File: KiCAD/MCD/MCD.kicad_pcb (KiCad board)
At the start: 2 copper layers, 197 x 101.5 mm, 76 parts, among them J1 DBUS_LOW, J2 DBUS_HIGH, J3 ABUS, J4 POWER, J5 JTAG, J6 Conn_01x02_Male, J7 DUART A, J8 DUART B, SW1 SW_Push, U1 XC9572XL-10VQG44C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

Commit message: control bus almost done
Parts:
- C1, C10, C11, C13, C2, C3, C4, C8, R10, R11, R14, R3, R4, R5, R6, R7: moved to B.Cu
- moved D2 55.6 mm to (106.5, 115.0), turned to 0 degrees
- moved D3 53.6 mm to (106.5, 118.0), turned to 0 degrees
- moved D4 51.9 mm to (106.5, 121.0), turned to 0 degrees
- moved D5 50.5 mm to (106.5, 124.0), turned to 0 degrees
- moved R17 50.2 mm to (110.9, 115.0), turned to 180 degrees
- moved D6 49.5 mm to (106.5, 127.0), turned to 0 degrees
- moved D7 48.8 mm to (106.5, 130.0), turned to 0 degrees
- moved R18 48.0 mm to (111.0, 118.0), turned to 180 degrees
- moved R19 46.1 mm to (111.0, 121.0), turned to 180 degrees
- moved R20 44.5 mm to (111.0, 124.0), turned to 180 degrees
- moved R21 43.3 mm to (111.0, 127.0), turned to 180 degrees
- moved R22 42.5 mm to (111.0, 130.0), turned to 180 degrees
- moved C8 10.7 mm to (253.0, 146.0)
- moved C2 10.7 mm to (280.0, 145.8)
- moved C10 10.5 mm to (198.5, 146.3)
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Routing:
- net RAMHCE: track 0.00 -> 190.1 mm, vias 0 -> 1
- net RAMHOE: track 0.00 -> 186.5 mm, vias 0 -> 1
- net ROMHCE: track 0.00 -> 160.5 mm, vias 0 -> 1
- net ROMHOE: track 0.00 -> 158.1 mm, vias 0 -> 1
- net RAMLCE: track 0.00 -> 134.4 mm, vias 0 -> 1
- net RAMLOE: track 0.00 -> 132.4 mm, vias 0 -> 1
- net RAMLCE2: track 162.4 -> 118.6 mm
- net R/W: track 248.4 -> 291.9 mm
- net RAMHCE2: track 208.0 -> 171.2 mm
- net ROMLOE: track 84.7 -> 110.6 mm, vias 3 -> 1
- net ROMLCE: track 87.9 -> 112.4 mm
- net +5V: track 86.1 -> 85.3 mm
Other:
- board size 197 x 101.5 mm -> 196.5 x 109.5 mm
- board text added: "GEORGE YACOUBIAN LETU SP 2024 GeorgeOS Single Board Computer - ADD FEET - ADD VETRIUM MARKERS - ADD ROUNDED CORNERS"
- board text removed: "GEORGE YACOUBIAN LETU SP 2024 GeorgeOS Single Board Computer - ADD FEET - ADD VETRIUM MARKERS - 4 LAYER?"

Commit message: update
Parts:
- moved J5 35.5 mm to (107.0, 136.5), turned to 90 degrees
- moved C20 27.0 mm to (118.0, 174.5), turned to 0 degrees
- moved U10 22.0 mm to (119.0, 171.0), turned to -90 degrees
- moved D3 15.1 mm to (117.8, 108.0)
- moved D4 15.1 mm to (117.8, 111.0)
- moved D5 15.1 mm to (117.8, 114.0)
- moved D6 15.1 mm to (117.8, 117.0)
- moved D7 15.1 mm to (117.8, 120.0)
- moved R17 15.1 mm to (122.2, 105.0)
- moved D2 15.1 mm to (117.7, 105.0)
- moved R18 15.1 mm to (122.2, 108.0)
- moved R19 15.1 mm to (122.2, 111.0)
- moved R20 15.1 mm to (122.2, 114.0)
- moved R21 15.1 mm to (122.2, 117.0)
- moved R22 15.1 mm to (122.2, 120.0)
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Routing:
- net RAMHCE2: track 171.2 -> 226.2 mm, vias 1 -> 2
- net RAMHCE: track 190.1 -> 237.1 mm
- net TDO: track 0.00 -> 46.9 mm, vias 0 -> 2
- net RAMHOE: track 186.5 -> 232.9 mm
- net SRESET: track 0.00 -> 31.3 mm, vias 0 -> 2
- net ROMHOE: track 158.1 -> 187.7 mm
- net BRESET: track 0.00 -> 24.2 mm, vias 0 -> 1
- net ROMHCE: track 160.5 -> 183.8 mm
- net TMS: track 0.00 -> 22.7 mm
- net TDI: track 0.00 -> 19.2 mm
- net RAMLOE: track 132.4 -> 150.8 mm
- net TCK: track 0.00 -> 18.0 mm
- net +5V: track 85.3 -> 102.9 mm, vias 6 -> 8
- net RAMLCE: track 134.4 -> 151.1 mm
- net RAMLCE2: track 118.6 -> 134.4 mm
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
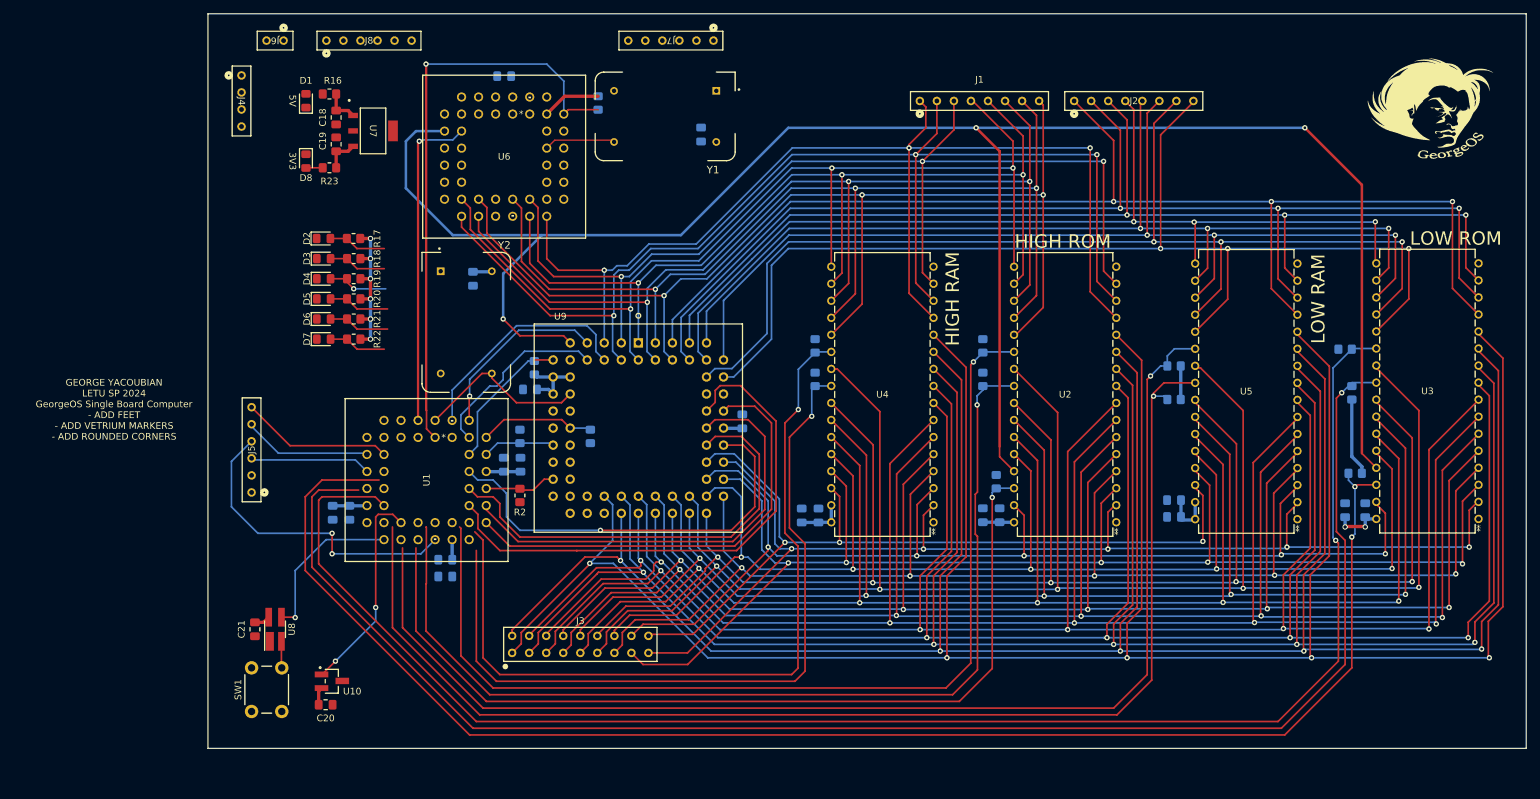
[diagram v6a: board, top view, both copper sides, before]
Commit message: everything but power connected
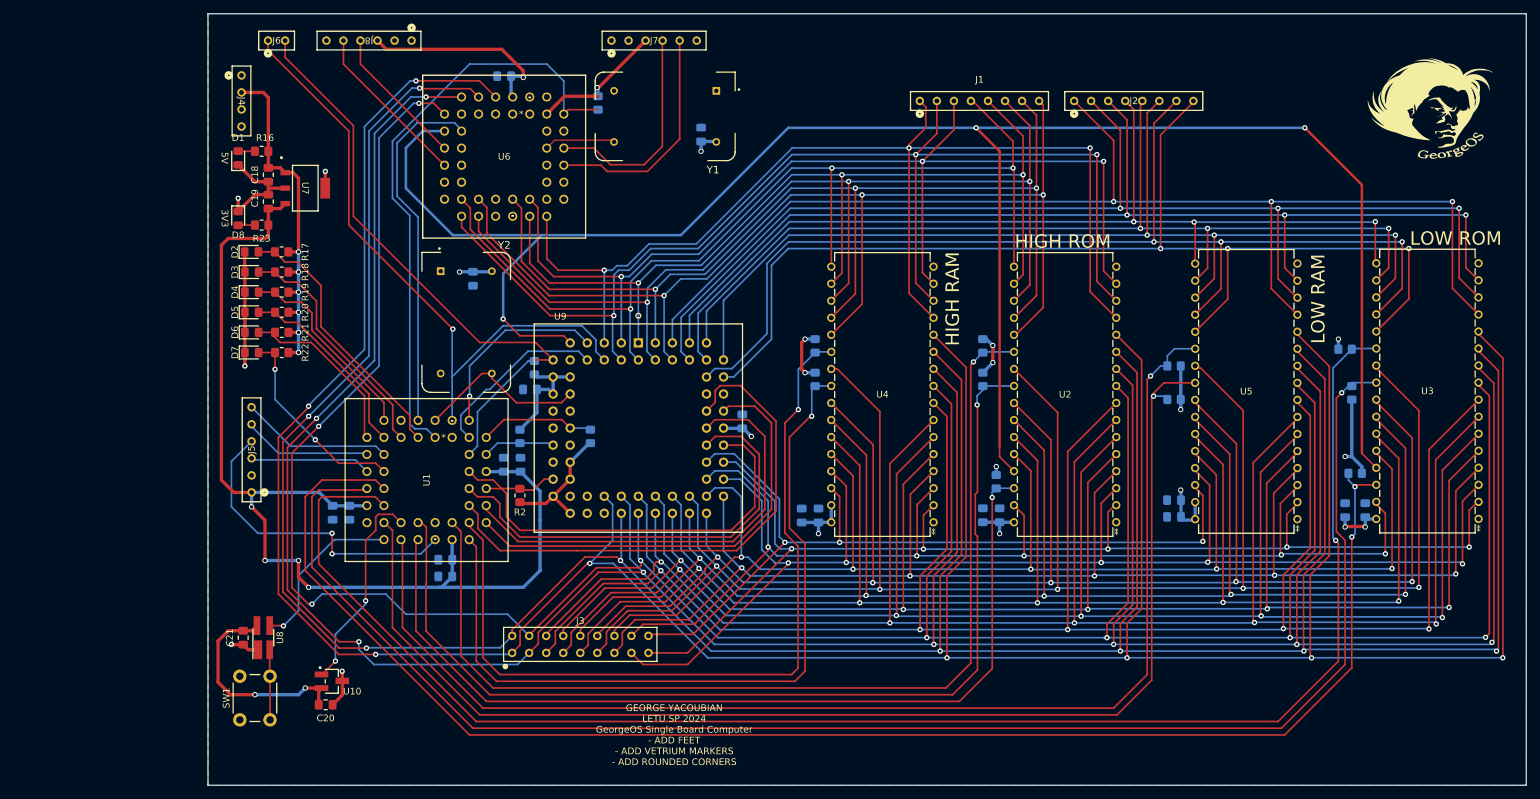
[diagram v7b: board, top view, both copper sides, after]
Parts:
- moved C18 13.2 mm to (109.5, 95.5)
- moved C19 13.2 mm to (109.5, 99.5)
- moved D1 13.2 mm to (105.0, 93.0)
- moved D8 13.2 mm to (105.0, 102.0)
- moved R16 13.2 mm to (108.5, 92.0)
- moved R23 13.2 mm to (108.5, 103.0)
- moved U7 13.2 mm to (115.0, 97.5)
- moved R17 10.9 mm to (111.5, 107.0)
- moved D2 10.9 mm to (107.0, 107.0)
- moved D3 10.9 mm to (107.0, 110.0)
- moved D4 10.9 mm to (107.0, 113.0)
- moved D5 10.9 mm to (107.0, 116.0)
- moved D6 10.9 mm to (107.0, 119.0)
- moved D7 10.9 mm to (107.0, 122.0)
- moved R18 10.9 mm to (111.5, 110.0)
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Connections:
- J6 pad 2: DTACK -> CPLD_DTACK
- U1 pad 12: RAMHOE -> LED5
- U1 pad 13: ROMHOE -> RAMHOE
- U1 pad 14: ROMHCE -> RAMHCE2
- U1 pad 19: RAMHCE2 -> ROMHOE
- U1 pad 20: LED0 -> ROMHCE
- U1 pad 22: LED1 -> RAMLCE2
- U1 pad 23: LED2 -> RAMLOE
- U1 pad 27: LED3 -> RAMLCE
- U1 pad 28: LED4 -> ROMLOE
- U1 pad 3: ROMLCE -> LED0
- U1 pad 30: LED5 -> ROMLCE
- U1 pad 5: RAMLCE -> LED1
- U1 pad 6: ROMLOE -> LED2
- U1 pad 7: RAMLCE2 -> LED4
- U1 pad 8: RAMLOE -> LED3
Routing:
- net +5V: track 102.9 -> 256.1 mm, vias 8 -> 26
- net +3V3: track 18.5 -> 158.0 mm, vias 0 -> 4
- net A1: track 374.4 -> 512.7 mm, vias 5 -> 8
- net A2: track 352.2 -> 485.8 mm, vias 5 -> 8
- net A3: track 338.9 -> 471.1 mm, vias 5 -> 8
- net A4: track 317.5 -> 443.5 mm, vias 5 -> 8
- net CPLD_DTACK: track 21.4 -> 90.4 mm
- net AS: track 34.8 -> 97.0 mm, vias 0 -> 1
- net GND: track 0.00 -> 47.9 mm, vias 0 -> 5
- net RXDA: track 0.00 -> 34.3 mm
- net TXDA: track 0.00 -> 32.6 mm
- net LED0: track 8.65 -> 40.0 mm
- net LED1: track 8.62 -> 36.0 mm
- net RXDB: track 0.00 -> 24.8 mm
- net LED5: track 8.62 -> 30.1 mm, vias 0 -> 2
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- added copper zone on B.Cu, net GND
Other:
- board size 196.5 x 109.5 mm -> 196.5 x 115 mm

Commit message: FINISHED!!! (I THINK)
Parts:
- added FID1: Fiducial, Fiducial:Fiducial_1.5mm_Mask3mm, F.Cu at (104.5, 75.5)
- added FID2: Fiducial, Fiducial:Fiducial_1.5mm_Mask3mm, F.Cu at (294.0, 74.5)
- added FID3: Fiducial, Fiducial:Fiducial_1.5mm_Mask3mm, F.Cu at (294.0, 183.5)
- added FID4: Fiducial, Fiducial:Fiducial_1.5mm_Mask3mm, B.Cu at (104.5, 75.5)
- added FID5: Fiducial, Fiducial:Fiducial_1.5mm_Mask3mm, B.Cu at (294.0, 183.5)
- added FID6: Fiducial, Fiducial:Fiducial_1.5mm_Mask3mm, B.Cu at (294.0, 74.5)
- moved C2 0.60 mm to (272.4, 145.4)
- moved U5 0.07 mm to (262.8, 146.8)
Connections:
- D1 pad 2: /3V3_LED -> /5V_LED
- R16 pad 2: /3V3_LED -> /5V_LED
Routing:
- net GND: track 47.9 -> 117.1 mm
- net RESET: track 10.8 -> 72.3 mm, vias 0 -> 3
- net +3V3: track 158.0 -> 188.2 mm
- net +5V: track 256.1 -> 277.0 mm, vias 26 -> 27
- net RAMHCE2: track 227.5 -> 232.7 mm
- net /5V_LED: track 0.00 -> 2.51 mm
- net /3V3_LED: track 5.02 -> 2.51 mm
- net DUARTCS: track 89.4 -> 88.4 mm, vias 0 -> 2
- net D14: track 165.9 -> 165.4 mm
- net D13: track 155.3 -> 154.8 mm
- net A19: track 62.6 -> 62.3 mm, vias 0 -> 1
- added copper zone on F.Cu, net +5V
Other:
- board size 196.5 x 115 mm -> 196.3 x 114.9 mm
- board text added: "+3V3"
- board text added: "+5V"
- board text added: "3.6864-MHZ CLOCK"
- board text added: "8-MHZ CLOCK"
- board text added: "A1"
- board text added: "A10"
- board text added: "A11"
- board text added: "A12"
- board text added: "A14"
- board text added: "A15"
- board text added: "A16"
- board text added: "A17"
- board text added: "A18"
- board text added: "A2"
- board text added: "A3"
- board text added: "A4"
- board text added: "A5"
- board text added: "A6"
- board text added: "A7"
- board text added: "A8"
- board text added: "A9"
- board text added: "AS"
- board text added: "CPLD"
- board text added: "CPU"
- board text added: "D0"
- board text added: "D1"
- board text added: "D10"
- board text added: "D11"
- board text added: "D12"
- board text added: "D13"
- board text added: "D14"
- board text added: "D15"
- board text added: "D2"
- board text added: "D3"
- board text added: "D4"
- board text added: "D5"
- board text added: "D6"
- board text added: "D7"
- board text added: "D8"
- board text added: "D9"
- board text added: "DOO-ART"
- board text added: "DTACK"
- board text added: "DUART CHANNEL A"
- board text added: "GEORGE YACOUBIAN LETU SP 2024 GeorgeOS Single Board Computer"
- board text added: "GND"
- board text added: "RESET"
- board text added: "RXA"
- board text added: "RXB"
- board text added: "TCK"
- board text added: "TDI"
- board text added: "TDO"
- board text added: "TMS"
- board text added: "TXA"
- board text added: "TXB"
- board text removed: "3V3"
- board text removed: "5V"
- board text removed: "GEORGE YACOUBIAN LETU SP 2024 GeorgeOS Single Board Computer - ADD FEET - ADD VETRIUM MARKERS - ADD ROUNDED CORNERS"
